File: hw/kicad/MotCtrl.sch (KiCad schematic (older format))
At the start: 0 parts

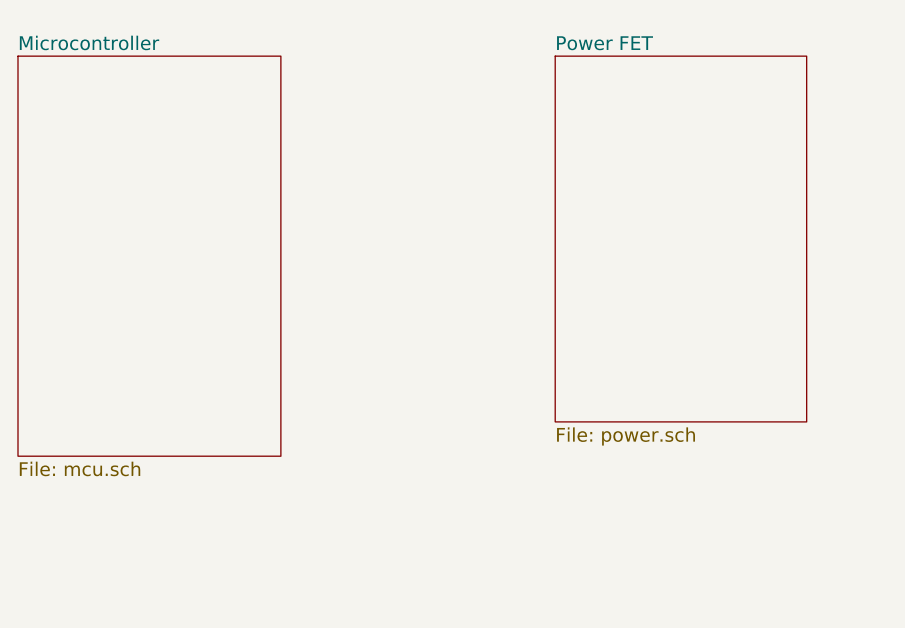
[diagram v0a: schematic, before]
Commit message: First steps on gate driver circuit
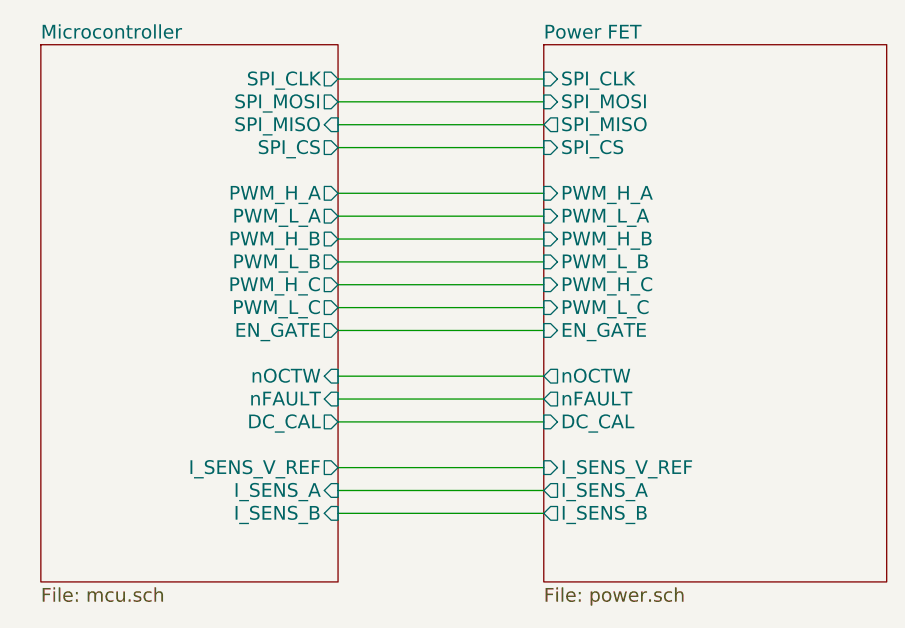
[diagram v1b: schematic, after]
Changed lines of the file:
@@
 $EndDescr
 $Sheet
-S 4650 2650 1150 1750
+S 4750 2600 1300 2350
 U 5815387E
 F0 "Microcontroller" 60
 F1 "mcu.sch" 60
+F2 "SPI_CLK" O R 6050 2750 60
+F3 "SPI_MOSI" O R 6050 2850 60
+F4 "SPI_MISO" I R 6050 2950 60
+F5 "SPI_CS" O R 6050 3050 60
+F6 "DC_CAL" O R 6050 4250 60
+F7 "nOCTW" I R 6050 4050 60
+F8 "nFAULT" I R 6050 4150 60
+F9 "PWM_H_A" O R 6050 3250 60
+F10 "PWM_L_A" O R 6050 3350 60
+F11 "PWM_H_B" O R 6050 3450 60
+F12 "PWM_L_B" O R 6050 3550 60
+F13 "PWM_H_C" O R 6050 3650 60
+F14 "PWM_L_C" O R 6050 3750 60
+F15 "EN_GATE" O R 6050 3850 60
+F16 "I_SENS_V_REF" O R 6050 4450 60
+F17 "I_SENS_A" I R 6050 4550 60
+F18 "I_SENS_B" I R 6050 4650 60
 $EndSheet
 $Sheet
-S 7000 2650 1100 1600
+S 6950 2600 1500 2350
 U 58153909
 F0 "Power FET" 60
 F1 "power.sch" 60
+F2 "SPI_CLK" I L 6950 2750 60
+F3 "SPI_MOSI" I L 6950 2850 60
+F4 "SPI_MISO" O L 6950 2950 60
+F5 "SPI_CS" I L 6950 3050 60
+F6 "PWM_H_A" I L 6950 3250 60
+F7 "PWM_L_A" I L 6950 3350 60
+F8 "PWM_H_B" I L 6950 3450 60
+F9 "PWM_L_B" I L 6950 3550 60
+F10 "PWM_H_C" I L 6950 3650 60
+F11 "PWM_L_C" I L 6950 3750 60
+F12 "EN_GATE" I L 6950 3850 60
+F13 "nOCTW" O L 6950 4050 60
+F14 "nFAULT" O L 6950 4150 60
+F15 "DC_CAL" I L 6950 4250 60
+F16 "I_SENS_V_REF" I L 6950 4450 60
+F17 "I_SENS_A" O L 6950 4550 60
+F18 "I_SENS_B" O L 6950 4650 60
 $EndSheet
+Wire Wire Line
+	6050 2750 6950 2750
+Wire Wire Line
+	6050 2850 6950 2850
+Wire Wire Line
+	6050 2950 6950 2950
+Wire Wire Line
+	6050 3050 6950 3050
+Wire Wire Line
+	6050 3250 6950 3250
+Wire Wire Line
+	6050 3350 6950 3350
+Wire Wire Line
+	6050 3450 6950 3450
+Wire Wire Line
+	6950 3550 6050 3550
+Wire Wire Line
+	6050 3650 6950 3650
+Wire Wire Line
+	6950 3750 6050 3750
+Wire Wire Line
+	6050 3850 6950 3850
+Wire Wire Line
+	6950 4050 6050 4050
+Wire Wire Line
+	6050 4150 6950 4150
+Wire Wire Line
+	6950 4250 6050 4250
+Wire Wire Line
+	6050 4450 6950 4450
+Wire Wire Line
+	6950 4550 6050 4550
+Wire Wire Line
+	6050 4650 6950 4650
 $EndSCHEMATC

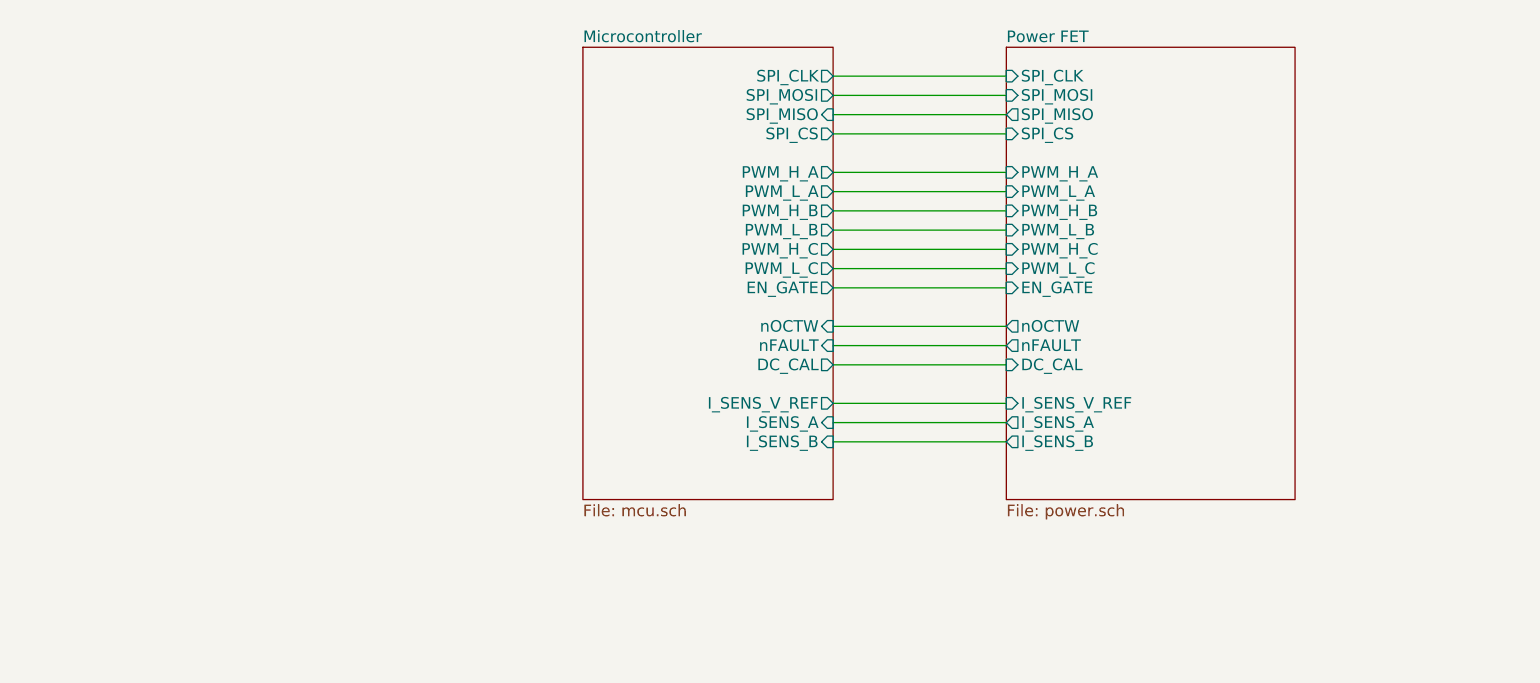
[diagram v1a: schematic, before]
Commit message: Some more work on the FET-stage
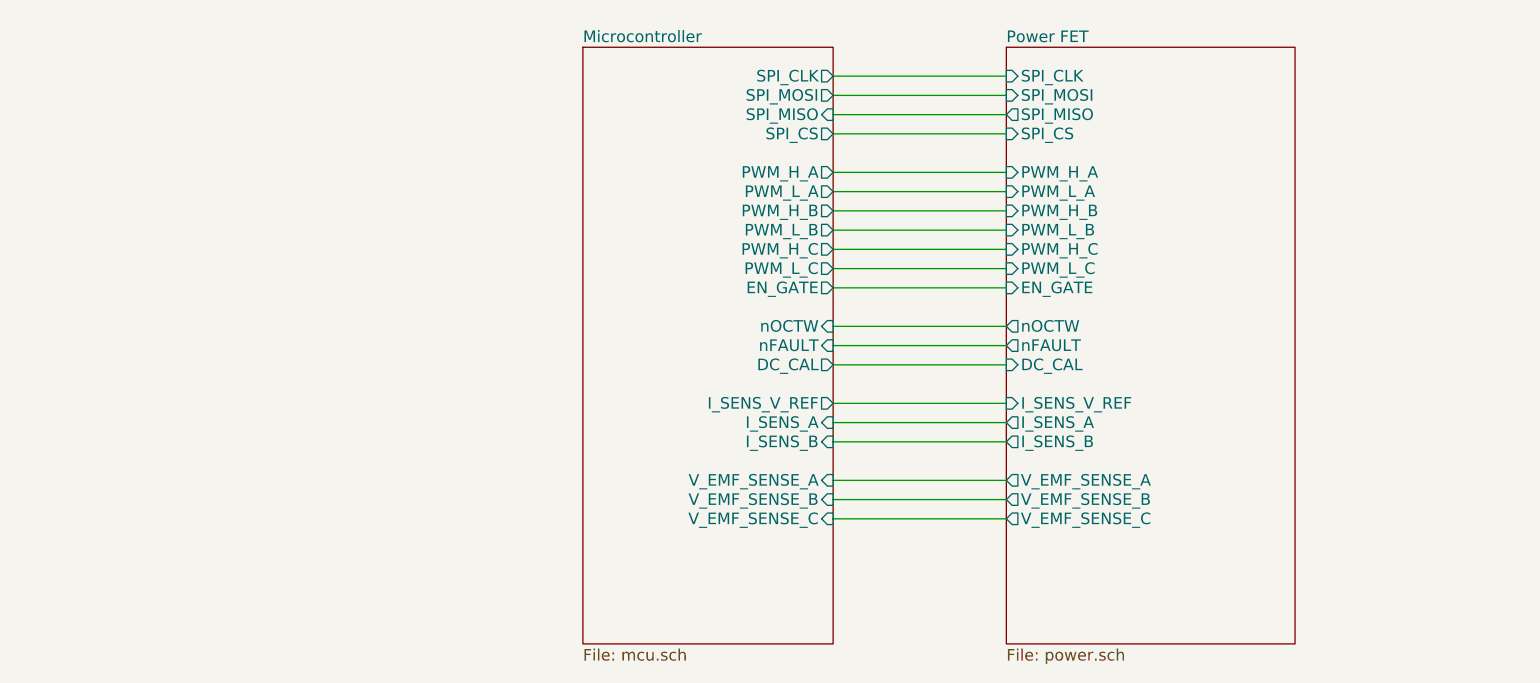
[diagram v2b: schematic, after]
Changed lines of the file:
@@
 $EndDescr
 $Sheet
-S 4750 2600 1300 2350
+S 4750 2600 1300 3100
 U 5815387E
 F0 "Microcontroller" 60
@@
 F17 "I_SENS_A" I R 6050 4550 60
 F18 "I_SENS_B" I R 6050 4650 60
+F19 "V_EMF_SENSE_A" I R 6050 4850 60
+F20 "V_EMF_SENSE_B" I R 6050 4950 60
+F21 "V_EMF_SENSE_C" I R 6050 5050 60
 $EndSheet
 $Sheet
-S 6950 2600 1500 2350
+S 6950 2600 1500 3100
 U 58153909
 F0 "Power FET" 60
@@
 F17 "I_SENS_A" O L 6950 4550 60
 F18 "I_SENS_B" O L 6950 4650 60
+F19 "V_EMF_SENSE_A" O L 6950 4850 60
+F20 "V_EMF_SENSE_B" O L 6950 4950 60
+F21 "V_EMF_SENSE_C" O L 6950 5050 60
 $EndSheet
 Wire Wire Line
@@
 Wire Wire Line
 	6050 4650 6950 4650
+Wire Wire Line
+	6050 4850 6950 4850
+Wire Wire Line
+	6950 4950 6050 4950
+Wire Wire Line
+	6050 5050 6950 5050
 $EndSCHEMATC

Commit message: More power work
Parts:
- added TP?: Phase A, Wire_Pads:SolderWirePad_single_SMD_5x10mm, symbol TESTPAD
- added TP?: Phase B, Wire_Pads:SolderWirePad_single_SMD_5x10mm, symbol TESTPAD
- added TP?: Phase C, Wire_Pads:SolderWirePad_single_SMD_5x10mm, symbol TESTPAD
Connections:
- new net Power FET/MOT_PH_A: TP?.1
- new net Power FET/MOT_PH_B: TP?.1
- new net Power FET/MOT_PH_C: TP?.1
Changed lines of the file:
@@
 LIBS:Zilog
 LIBS:drv8301
+LIBS:wslp2726
+LIBS:test
 LIBS:MotCtrl-cache
 EELAYER 25 0
@@
 F20 "V_EMF_SENSE_B" I R 6050 4950 60
 F21 "V_EMF_SENSE_C" I R 6050 5050 60
+F22 "V_BAT_SENSE" I R 6050 5250 60
 $EndSheet
 $Sheet
@@
 F20 "V_EMF_SENSE_B" O L 6950 4950 60
 F21 "V_EMF_SENSE_C" O L 6950 5050 60
+F22 "MOT_PH_A" O R 8450 3250 60
+F23 "MOT_PH_B" O R 8450 3350 60
+F24 "MOT_PH_C" O R 8450 3450 60
+F25 "V_BAT_SENSE" O L 6950 5250 60
 $EndSheet
 Wire Wire Line
@@
 Wire Wire Line
 	6050 5050 6950 5050
+Wire Wire Line
+	6050 5250 6950 5250
+$Comp
+L TESTPAD TP?
+U 1 1 581F3C20
+P 9250 3250
+F 0 "TP?" V 9200 3200 40  0000 C CNN
+F 1 "Phase A" V 9250 3500 40  0000 C CNN
+F 2 "Wire_Pads:SolderWirePad_single_SMD_5x10mm" V 9250 3400 60  0001 C CNN
+F 3 "" V 9250 3400 60  0000 C CNN
+	1    9250 3250
+	0    1    1    0
+$EndComp
+Wire Wire Line
+	8450 3250 9200 3250
+Wire Wire Line
+	8450 3450 9200 3450
+Wire Wire Line
+	9200 3350 8450 3350
+$Comp
+L TESTPAD TP?
+U 1 1 581F8700
+P 9250 3350
+F 0 "TP?" V 9200 3300 40  0000 C CNN
+F 1 "Phase B" V 9250 3600 40  0000 C CNN
+F 2 "Wire_Pads:SolderWirePad_single_SMD_5x10mm" V 9250 3500 60  0001 C CNN
+F 3 "" V 9250 3500 60  0000 C CNN
+	1    9250 3350
+	0    1    1    0
+$EndComp
+$Comp
+L TESTPAD TP?
+U 1 1 581F8822
+P 9250 3450
+F 0 "TP?" V 9200 3400 40  0000 C CNN
+F 1 "Phase C" V 9250 3700 40  0000 C CNN
+F 2 "Wire_Pads:SolderWirePad_single_SMD_5x10mm" V 9250 3600 60  0001 C CNN
+F 3 "" V 9250 3600 60  0000 C CNN
+	1    9250 3450
+	0    1    1    0
+$EndComp
 $EndSCHEMATC

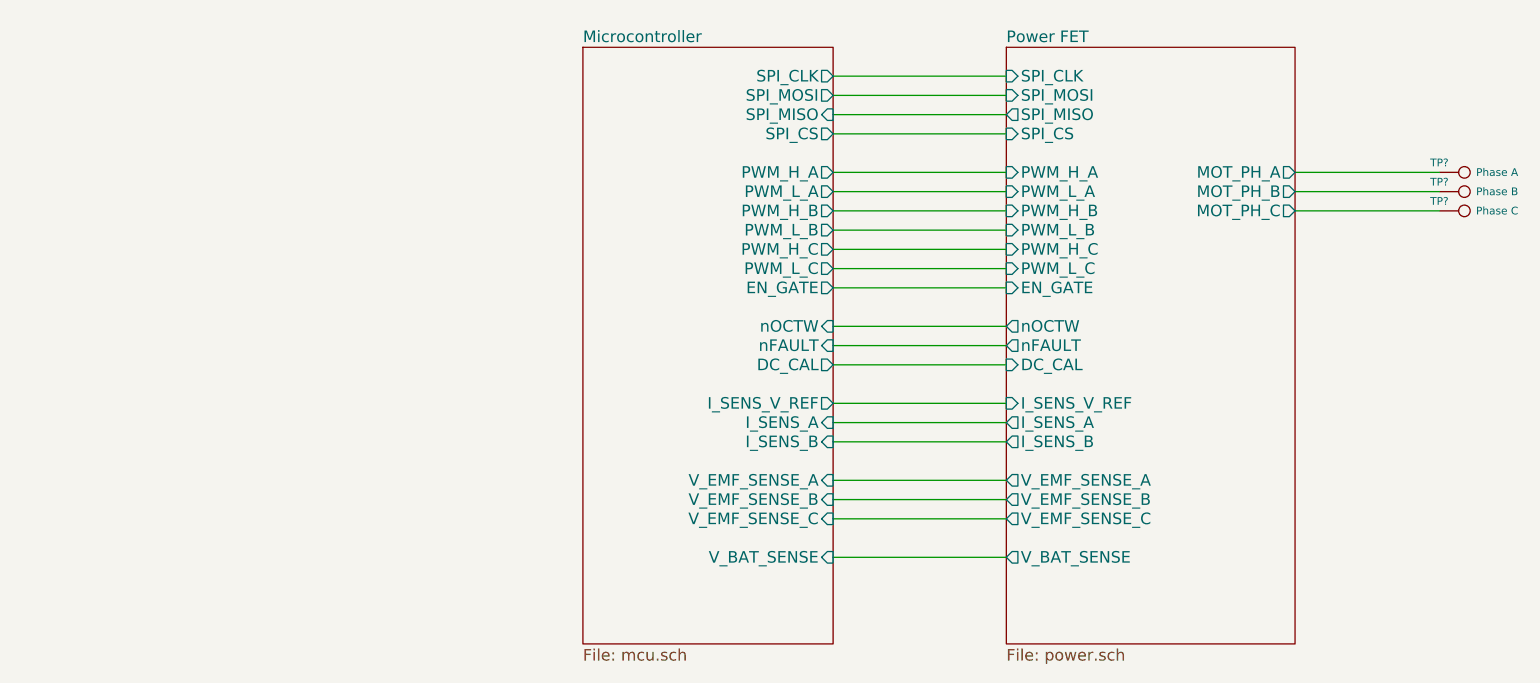
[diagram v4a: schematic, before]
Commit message: Big changes in power: new mosfets, drivers and current sensing
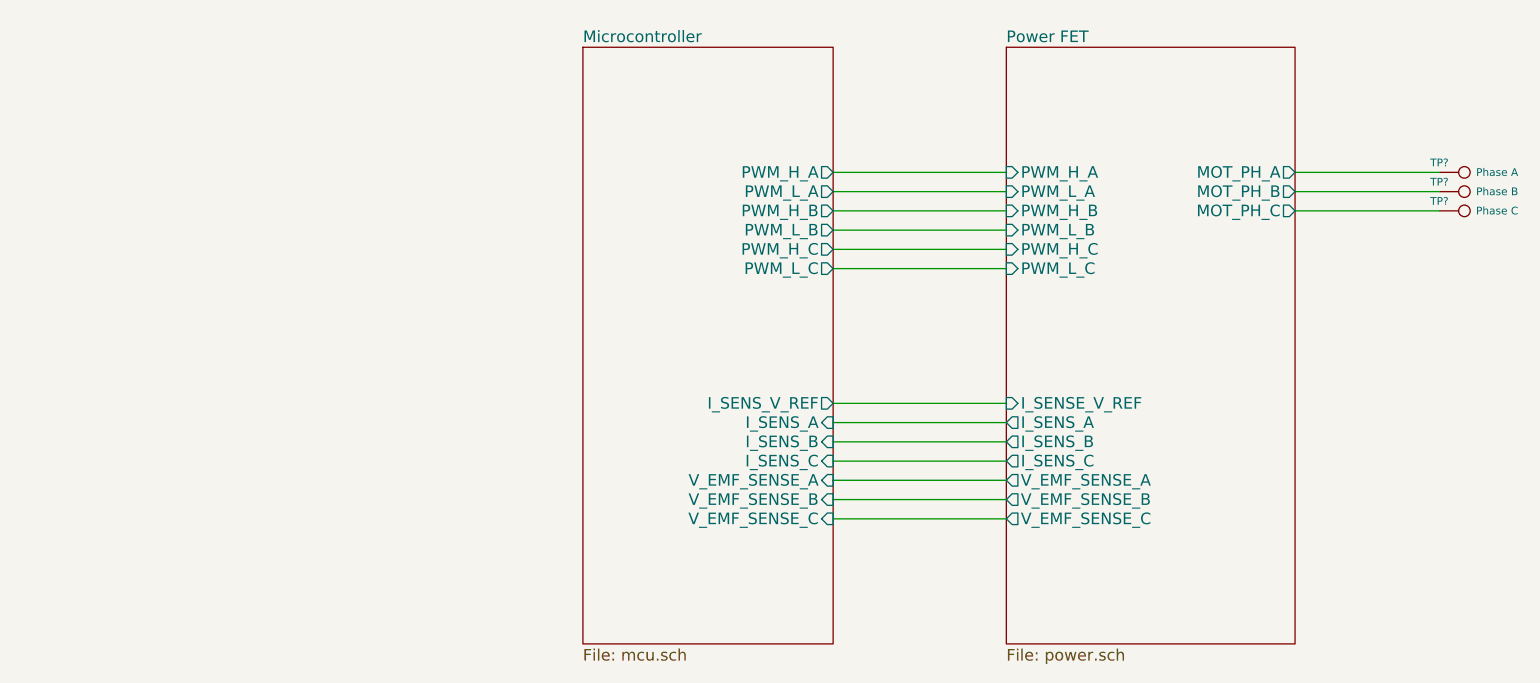
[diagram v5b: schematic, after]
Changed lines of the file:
@@
 LIBS:test
 LIBS:az1117c
+LIBS:ina240
+LIBS:FDBL0110N60
+LIBS:lm5101a
 LIBS:MotCtrl-cache
 EELAYER 25 0
@@
 F0 "Microcontroller" 60
 F1 "mcu.sch" 60
-F2 "SPI_CLK" O R 6050 2750 60
-F3 "SPI_MOSI" O R 6050 2850 60
-F4 "SPI_MISO" I R 6050 2950 60
-F5 "SPI_CS" O R 6050 3050 60
-F6 "DC_CAL" O R 6050 4250 60
-F7 "nOCTW" I R 6050 4050 60
-F8 "nFAULT" I R 6050 4150 60
-F9 "PWM_H_A" O R 6050 3250 60
-F10 "PWM_L_A" O R 6050 3350 60
-F11 "PWM_H_B" O R 6050 3450 60
-F12 "PWM_L_B" O R 6050 3550 60
-F13 "PWM_H_C" O R 6050 3650 60
-F14 "PWM_L_C" O R 6050 3750 60
-F15 "EN_GATE" O R 6050 3850 60
-F16 "I_SENS_V_REF" O R 6050 4450 60
-F17 "I_SENS_A" I R 6050 4550 60
-F18 "I_SENS_B" I R 6050 4650 60
-F19 "V_EMF_SENSE_A" I R 6050 4850 60
-F20 "V_EMF_SENSE_B" I R 6050 4950 60
-F21 "V_EMF_SENSE_C" I R 6050 5050 60
-F22 "V_BAT_SENSE" I R 6050 5250 60
+F2 "PWM_H_A" O R 6050 3250 60
+F3 "PWM_L_A" O R 6050 3350 60
+F4 "PWM_H_B" O R 6050 3450 60
+F5 "PWM_L_B" O R 6050 3550 60
+F6 "PWM_H_C" O R 6050 3650 60
+F7 "PWM_L_C" O R 6050 3750 60
+F8 "I_SENS_V_REF" O R 6050 4450 60
+F9 "I_SENS_A" I R 6050 4550 60
+F10 "I_SENS_B" I R 6050 4650 60
+F11 "V_EMF_SENSE_A" I R 6050 4850 60
+F12 "V_EMF_SENSE_B" I R 6050 4950 60
+F13 "V_EMF_SENSE_C" I R 6050 5050 60
+F14 "I_SENS_C" I R 6050 4750 60
 $EndSheet
 $Sheet
@@
 F0 "Power FET" 60
 F1 "power.sch" 60
-F2 "SPI_CLK" I L 6950 2750 60
-F3 "SPI_MOSI" I L 6950 2850 60
-F4 "SPI_MISO" O L 6950 2950 60
-F5 "SPI_CS" I L 6950 3050 60
-F6 "PWM_H_A" I L 6950 3250 60
-F7 "PWM_L_A" I L 6950 3350 60
-F8 "PWM_H_B" I L 6950 3450 60
-F9 "PWM_L_B" I L 6950 3550 60
-F10 "PWM_H_C" I L 6950 3650 60
-F11 "PWM_L_C" I L 6950 3750 60
-F12 "EN_GATE" I L 6950 3850 60
-F13 "nOCTW" O L 6950 4050 60
-F14 "nFAULT" O L 6950 4150 60
-F15 "DC_CAL" I L 6950 4250 60
-F16 "I_SENS_V_REF" I L 6950 4450 60
-F17 "I_SENS_A" O L 6950 4550 60
-F18 "I_SENS_B" O L 6950 4650 60
-F19 "V_EMF_SENSE_A" O L 6950 4850 60
-F20 "V_EMF_SENSE_B" O L 6950 4950 60
-F21 "V_EMF_SENSE_C" O L 6950 5050 60
-F22 "MOT_PH_A" O R 8450 3250 60
-F23 "MOT_PH_B" O R 8450 3350 60
-F24 "MOT_PH_C" O R 8450 3450 60
-F25 "V_BAT_SENSE" O L 6950 5250 60
+F2 "PWM_H_A" I L 6950 3250 60
+F3 "PWM_L_A" I L 6950 3350 60
+F4 "PWM_H_B" I L 6950 3450 60
+F5 "PWM_L_B" I L 6950 3550 60
+F6 "PWM_H_C" I L 6950 3650 60
+F7 "PWM_L_C" I L 6950 3750 60
+F8 "I_SENS_A" O L 6950 4550 60
+F9 "I_SENS_B" O L 6950 4650 60
+F10 "V_EMF_SENSE_A" O L 6950 4850 60
+F11 "V_EMF_SENSE_B" O L 6950 4950 60
+F12 "V_EMF_SENSE_C" O L 6950 5050 60
+F13 "MOT_PH_A" O R 8450 3250 60
+F14 "MOT_PH_B" O R 8450 3350 60
+F15 "MOT_PH_C" O R 8450 3450 60
+F16 "I_SENSE_V_REF" I L 6950 4450 60
+F17 "I_SENS_C" O L 6950 4750 60
 $EndSheet
-Wire Wire Line
-	6050 2750 6950 2750
-Wire Wire Line
-	6050 2850 6950 2850
-Wire Wire Line
-	6050 2950 6950 2950
-Wire Wire Line
-	6050 3050 6950 3050
 Wire Wire Line
 	6050 3250 6950 3250
@@
 	6950 3750 6050 3750
 Wire Wire Line
-	6050 3850 6950 3850
-Wire Wire Line
-	6950 4050 6050 4050
-Wire Wire Line
-	6050 4150 6950 4150
-Wire Wire Line
-	6950 4250 6050 4250
-Wire Wire Line
 	6050 4450 6950 4450
 Wire Wire Line
@@
 Wire Wire Line
 	6050 5050 6950 5050
-Wire Wire Line
-	6050 5250 6950 5250
 $Comp
 L TESTPAD TP?
@@
 	0    1    1    0
 $EndComp
+Wire Wire Line
+	6050 4750 6950 4750
 $EndSCHEMATC

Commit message: Started working on power supplies
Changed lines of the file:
@@
 LIBS:FDBL0110N60
 LIBS:lm5101a
+LIBS:LM22675
 LIBS:MotCtrl-cache
 EELAYER 25 0
@@
 $Descr A4 11693 8268
 encoding utf-8
-Sheet 1 3
+Sheet 1 4
 Title ""
 Date ""
@@
 Wire Wire Line
 	6050 4750 6950 4750
+$Sheet
+S 1800 2550 1600 2050
+U 582A5C38
+F0 "Power Supply" 60
+F1 "power_supply.sch" 60
+$EndSheet
 $EndSCHEMATC

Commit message: Gate power supply enabling and board temp sensor
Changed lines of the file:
@@
 F13 "V_EMF_SENSE_C" I R 6050 5050 60
 F14 "I_SENS_C" I R 6050 4750 60
+F15 "GATE_PWR_EN" O L 4750 3250 60
 $EndSheet
 $Sheet
@@
 F0 "Power Supply" 60
 F1 "power_supply.sch" 60
+F2 "GATE_PWR_EN" I R 3400 3250 60
 $EndSheet
+Wire Wire Line
+	3400 3250 4750 3250
 $EndSCHEMATC
